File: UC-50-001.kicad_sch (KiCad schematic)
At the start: 0 parts

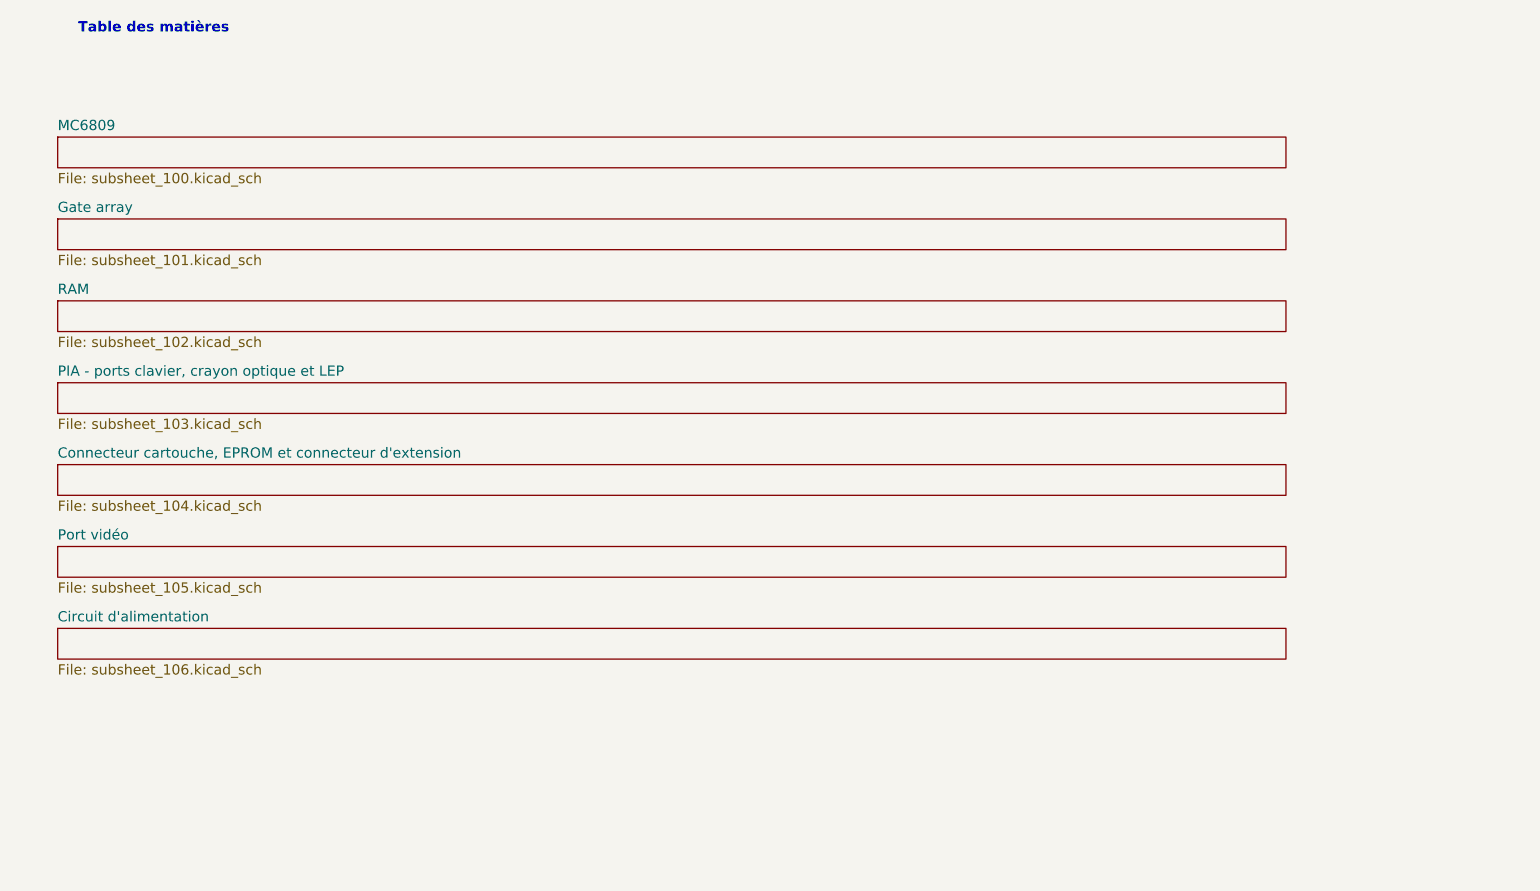
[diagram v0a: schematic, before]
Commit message: place les principaux circuits -- il manque le symbole pour le PIA MC6821
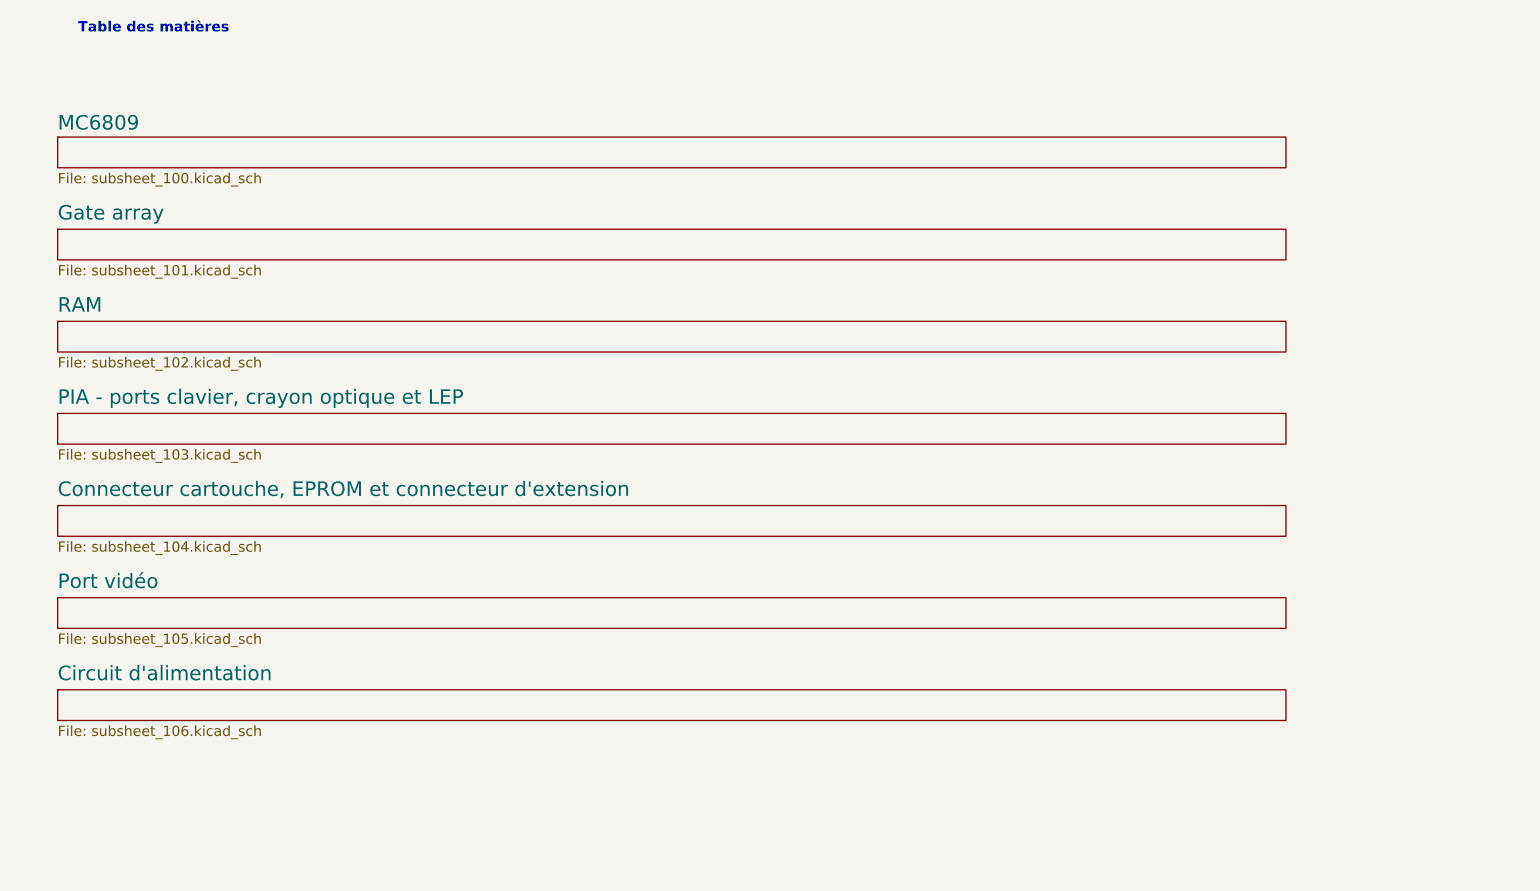
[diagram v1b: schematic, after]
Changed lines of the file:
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@@
     (effects (font (size 1.27 1.27) (thickness 0.254) bold) (justify left bottom))
   )
-  (sheet (at 35.56 88.9) (size 152.4 3.81) (fields_autoplaced)
+  (sheet (at 35.56 95.25) (size 152.4 3.81) (fields_autoplaced)
     (stroke (width 0.1524) (type solid) (color 0 0 0 0))
     (fill (color 0 0 0 0.0000))
-    (property "Sheet name" "Port vidéo" (id 0) (at 35.56 88.1884 0)
-      (effects (font (size 1.27 1.27)) (justify left bottom))
+    (property "Sheet name" "Port vidéo" (id 0) (at 35.56 94.2734 0)
+      (effects (font (size 1.8 1.8)) (justify left bottom))
     )
-    (property "Sheet file" "subsheet_105.kicad_sch" (id 1) (at 35.56 93.2946 0)
+    (property "Sheet file" "subsheet_105.kicad_sch" (id 1) (at 35.56 99.6446 0)
       (effects (font (size 1.27 1.27)) (justify left top))
     )
   )
-  (sheet (at 35.56 58.42) (size 152.4 3.81) (fields_autoplaced)
+  (sheet (at 35.56 60.96) (size 152.4 3.81) (fields_autoplaced)
     (stroke (width 0.1524) (type solid) (color 0 0 0 0))
     (fill (color 0 0 0 0.0000))
-    (property "Sheet name" "RAM" (id 0) (at 35.56 57.7084 0)
-      (effects (font (size 1.27 1.27)) (justify left bottom))
+    (property "Sheet name" "RAM" (id 0) (at 35.56 59.9834 0)
+      (effects (font (size 1.8 1.8)) (justify left bottom))
     )
-    (property "Sheet file" "subsheet_102.kicad_sch" (id 1) (at 35.56 62.8146 0)
+    (property "Sheet file" "subsheet_102.kicad_sch" (id 1) (at 35.56 65.3546 0)
       (effects (font (size 1.27 1.27)) (justify left top))
     )
   )
-  (sheet (at 35.56 99.06) (size 152.4 3.81) (fields_autoplaced)
+  (sheet (at 35.56 106.68) (size 152.4 3.81) (fields_autoplaced)
     (stroke (width 0.1524) (type solid) (color 0 0 0 0))
     (fill (color 0 0 0 0.0000))
-    (property "Sheet name" "Circuit d'alimentation" (id 0) (at 35.56 98.3484 0)
-      (effects (font (size 1.27 1.27)) (justify left bottom))
+    (property "Sheet name" "Circuit d'alimentation" (id 0) (at 35.56 105.7034 0)
+      (effects (font (size 1.8 1.8)) (justify left bottom))
     )
-    (property "Sheet file" "subsheet_106.kicad_sch" (id 1) (at 35.56 103.4546 0)
+    (property "Sheet file" "subsheet_106.kicad_sch" (id 1) (at 35.56 111.0746 0)
       (effects (font (size 1.27 1.27)) (justify left top))
     )
@@
     (fill (color 0 0 0 0.0000))
     (property "Sheet name" "MC6809" (id 0) (at 35.56 37.3884 0)
-      (effects (font (size 1.27 1.27)) (justify left bottom))
+      (effects (font (size 1.8 1.8)) (justify left bottom))
     )
     (property "Sheet file" "subsheet_100.kicad_sch" (id 1) (at 35.56 42.4946 0)
@@
     )
   )
-  (sheet (at 35.56 68.58) (size 152.4 3.81) (fields_autoplaced)
+  (sheet (at 35.56 72.39) (size 152.4 3.81) (fields_autoplaced)
     (stroke (width 0.1524) (type solid) (color 0 0 0 0))
     (fill (color 0 0 0 0.0000))
-    (property "Sheet name" "PIA - ports clavier, crayon optique et LEP" (id 0) (at 35.56 67.8684 0)
-      (effects (font (size 1.27 1.27)) (justify left bottom))
+    (property "Sheet name" "PIA - ports clavier, crayon optique et LEP" (id 0) (at 35.56 71.4134 0)
+      (effects (font (size 1.8 1.8)) (justify left bottom))
     )
-    (property "Sheet file" "subsheet_103.kicad_sch" (id 1) (at 35.56 72.9746 0)
+    (property "Sheet file" "subsheet_103.kicad_sch" (id 1) (at 35.56 76.7846 0)
       (effects (font (size 1.27 1.27)) (justify left top))
     )
   )
-  (sheet (at 35.56 78.74) (size 152.4 3.81) (fields_autoplaced)
+  (sheet (at 35.56 83.82) (size 152.4 3.81) (fields_autoplaced)
     (stroke (width 0.1524) (type solid) (color 0 0 0 0))
     (fill (color 0 0 0 0.0000))
-    (property "Sheet name" "Connecteur cartouche, EPROM et connecteur d'extension" (id 0) (at 35.56 78.0284 0)
-      (effects (font (size 1.27 1.27)) (justify left bottom))
+    (property "Sheet name" "Connecteur cartouche, EPROM et connecteur d'extension" (id 0) (at 35.56 82.8434 0)
+      (effects (font (size 1.8 1.8)) (justify left bottom))
     )
-    (property "Sheet file" "subsheet_104.kicad_sch" (id 1) (at 35.56 83.1346 0)
+    (property "Sheet file" "subsheet_104.kicad_sch" (id 1) (at 35.56 88.2146 0)
       (effects (font (size 1.27 1.27)) (justify left top))
     )
   )
-  (sheet (at 35.56 48.26) (size 152.4 3.81) (fields_autoplaced)
+  (sheet (at 35.56 49.53) (size 152.4 3.81) (fields_autoplaced)
     (stroke (width 0.1524) (type solid) (color 0 0 0 0))
     (fill (color 0 0 0 0.0000))
-    (property "Sheet name" "Gate array" (id 0) (at 35.56 47.5484 0)
-      (effects (font (size 1.27 1.27)) (justify left bottom))
+    (property "Sheet name" "Gate array" (id 0) (at 35.56 48.5534 0)
+      (effects (font (size 1.8 1.8)) (justify left bottom))
     )
-    (property "Sheet file" "subsheet_101.kicad_sch" (id 1) (at 35.56 52.6546 0)
+    (property "Sheet file" "subsheet_101.kicad_sch" (id 1) (at 35.56 53.9246 0)
       (effects (font (size 1.27 1.27)) (justify left top))
     )
@@
   )
   (symbol_instances
+    (path "/3b9df46e-3592-4470-9765-1c36c3c4b1c2/1425be50-4ffe-4685-9900-caf49649b930"
+      (reference "U?") (unit 1) (value "16384-WORD_BY_4-BIT_DYNAMIC_RAM_PHY") (footprint "Package_DIP:DIP-18_W7.62mm_LongPads")
+    )
+    (path "/f465a4b1-7c3c-40cc-9e66-ff9f17003d42/2edb98bf-6c70-4551-a503-f7af487edfe6"
+      (reference "U?") (unit 1) (value "GATE_ARRAY_MO5_V1_PHY") (footprint "Package_LCC:PLCC-68_THT-Socket")
+    )
+    (path "/3b9df46e-3592-4470-9765-1c36c3c4b1c2/45f1b914-2512-4187-bc68-201a3ab3400f"
+      (reference "U?") (unit 1) (value "16384-WORD_BY_4-BIT_DYNAMIC_RAM_PHY") (footprint "Package_DIP:DIP-18_W7.62mm_LongPads")
+    )
     (path "/afd59d07-bfd6-4bc9-8176-e0ddec1872a1/63085d07-f111-48f0-9996-774660e796f0"
       (reference "U?") (unit 1) (value "8-BIT_MICROPROCESSING_UNIT_6809_PHY") (footprint "Package_DIP:DIP-40_W15.24mm_LongPads")
     )
+    (path "/3b9df46e-3592-4470-9765-1c36c3c4b1c2/72713eb8-f847-4a8e-81bf-25e460104e73"
+      (reference "U?") (unit 1) (value "16384-WORD_BY_4-BIT_DYNAMIC_RAM_PHY") (footprint "Package_DIP:DIP-18_W7.62mm_LongPads")
+    )
+    (path "/3b9df46e-3592-4470-9765-1c36c3c4b1c2/bf3fae33-4051-45dd-9d68-60d6a697af51"
+      (reference "U?") (unit 1) (value "16384-WORD_BY_4-BIT_DYNAMIC_RAM_PHY") (footprint "Package_DIP:DIP-18_W7.62mm_LongPads")
+    )
+    (path "/3b9df46e-3592-4470-9765-1c36c3c4b1c2/dcf32591-7294-4bb0-9cab-321c99a5c1ff"
+      (reference "U?") (unit 1) (value "16384-WORD_BY_4-BIT_DYNAMIC_RAM_PHY") (footprint "Package_DIP:DIP-18_W7.62mm_LongPads")
+    )
+    (path "/3b9df46e-3592-4470-9765-1c36c3c4b1c2/edf7d0d1-1070-4c87-a709-1d85f3bb622c"
+      (reference "U?") (unit 1) (value "16384-WORD_BY_4-BIT_DYNAMIC_RAM_PHY") (footprint "Package_DIP:DIP-18_W7.62mm_LongPads")
+    )
   )
